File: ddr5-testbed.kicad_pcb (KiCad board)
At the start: 6 copper layers, 69.6 x 30 mm, 64 parts, among them IC1 PCA6408APW, IC2 AT24CS01, J1 ddr4-sodimm-edge-connector, U1 MT60B2G8HB-48B_A, U2 TPS613221ADBVT

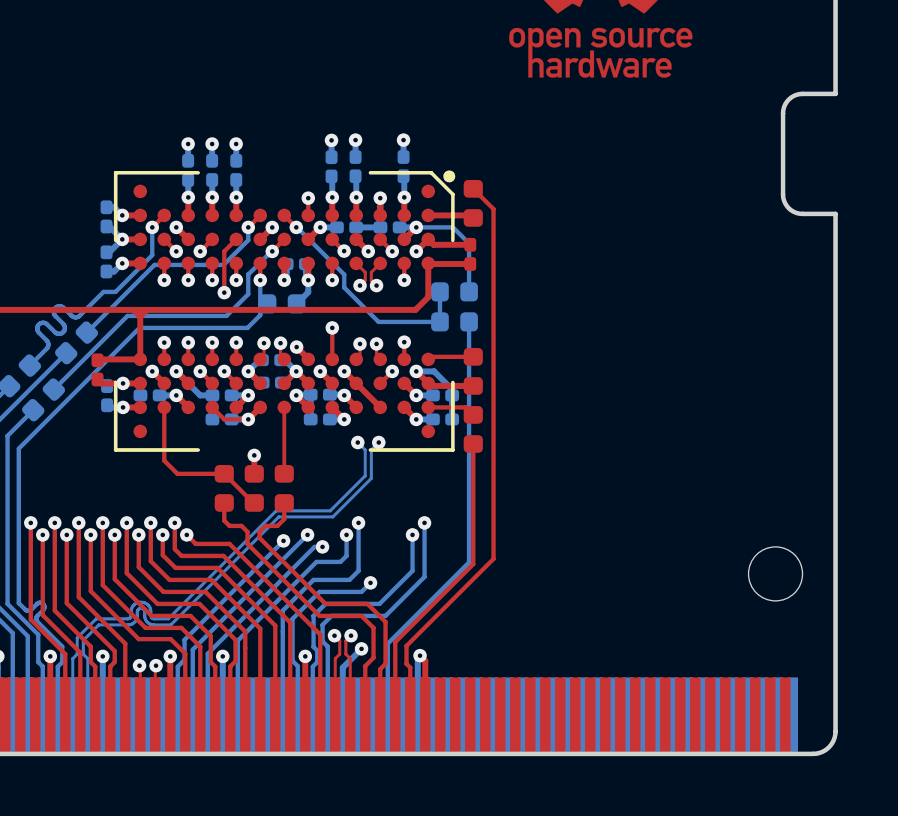
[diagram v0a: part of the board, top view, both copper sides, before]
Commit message: Tune LBDQ traces
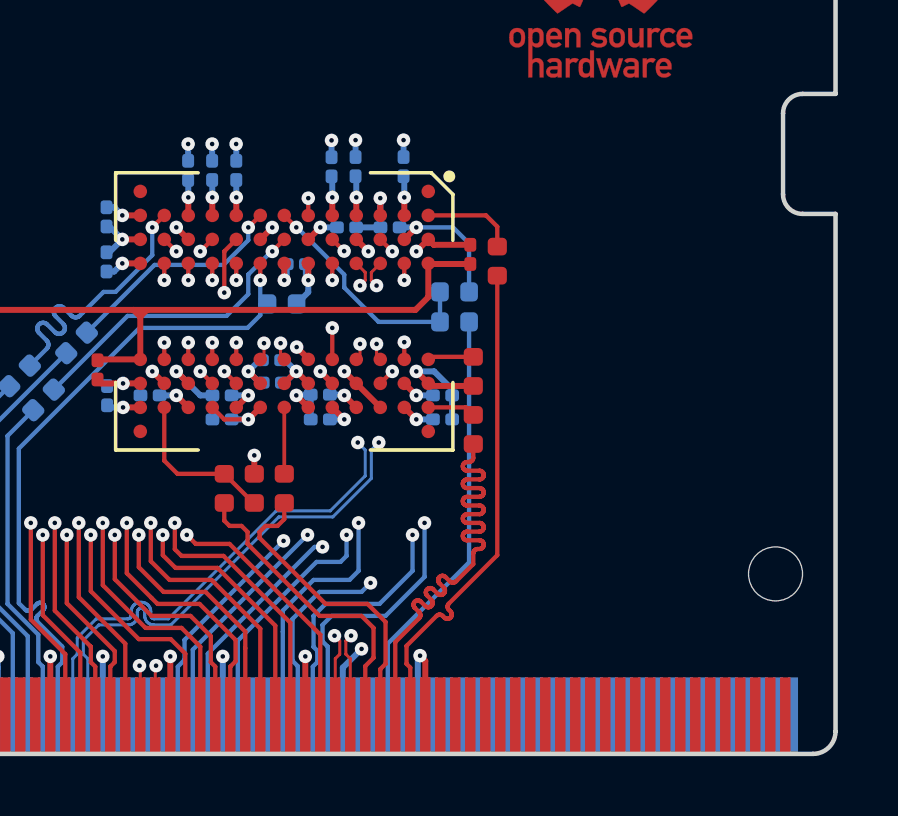
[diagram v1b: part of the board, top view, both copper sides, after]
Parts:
- moved R18 2.08 mm to (158.3, 83.6), turned to 270 degrees
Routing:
- net LBDQS: track 10.1 -> 18.0 mm
- net LBDQ: track 19.1 -> 16.4 mm
- net /DDR5/R_LBDQ: track 1.54 -> 3.12 mm

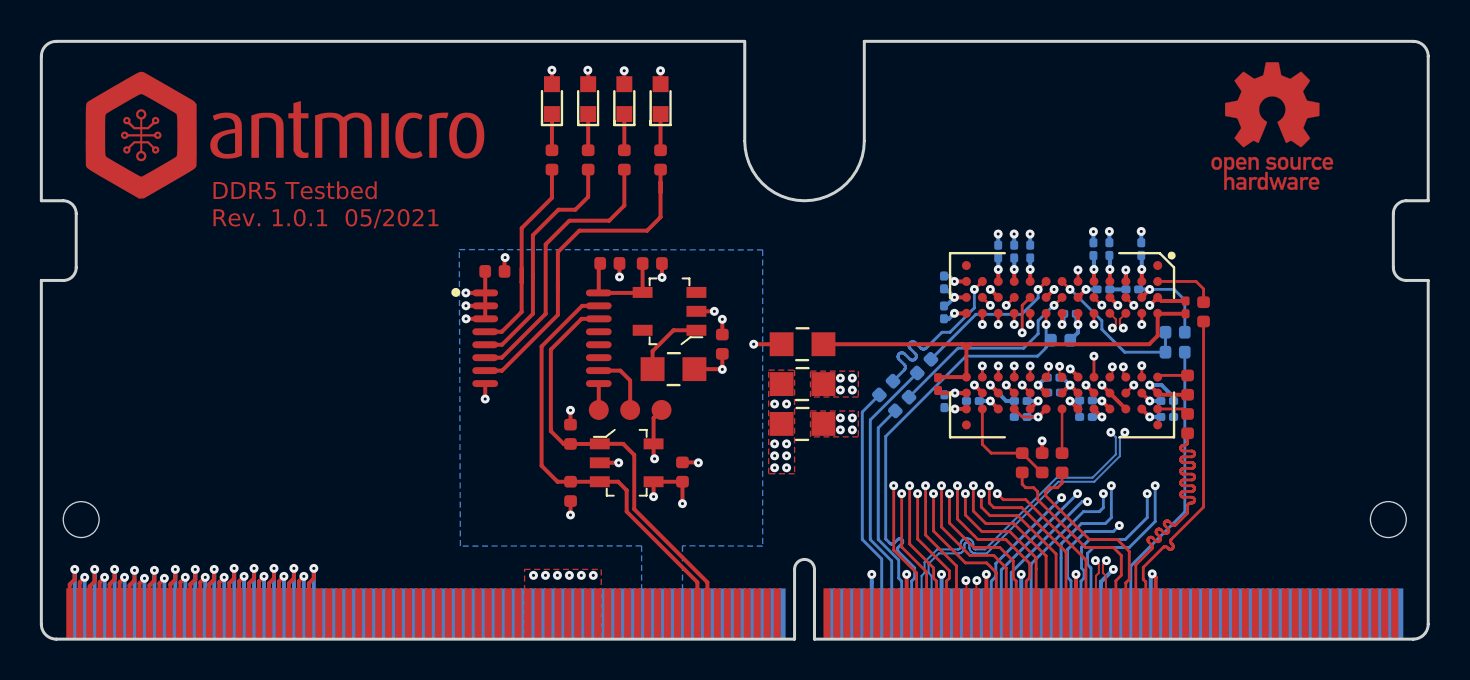
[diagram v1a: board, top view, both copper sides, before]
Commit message: Silks cleanup, fix date text
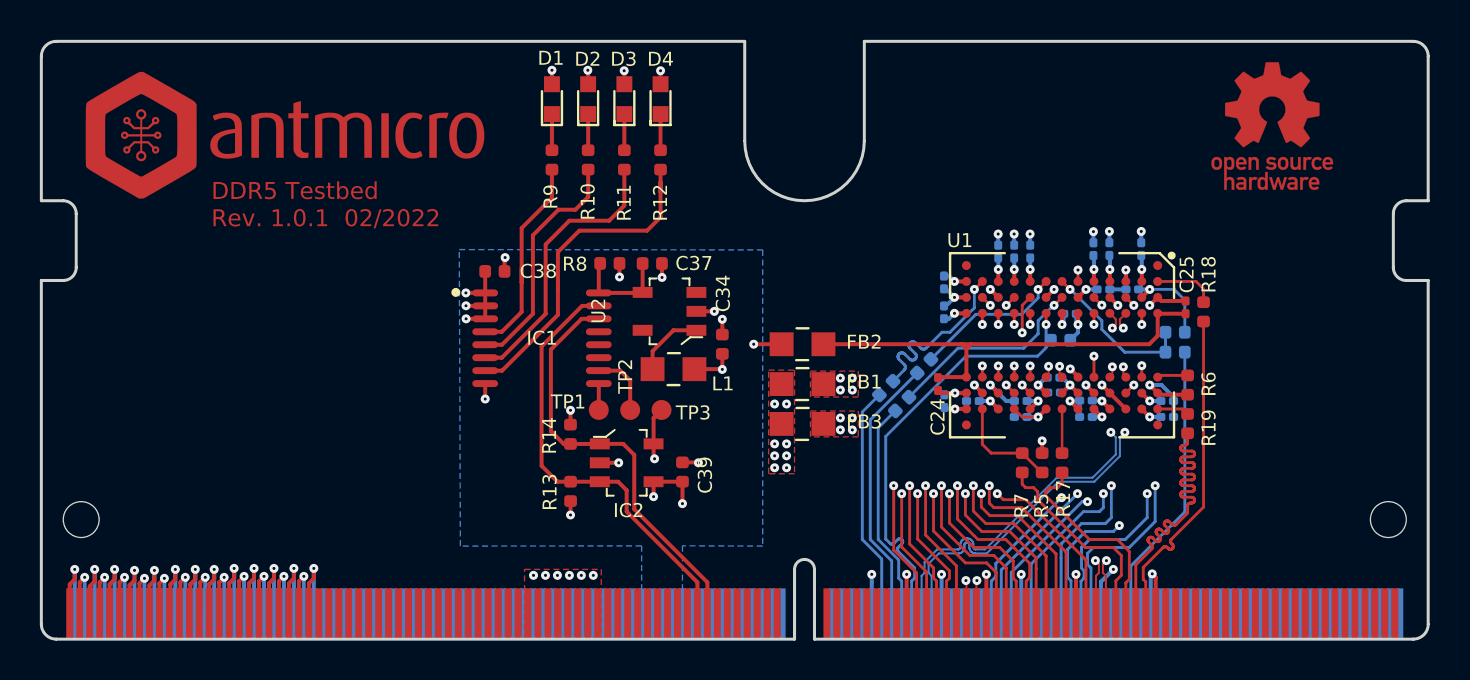
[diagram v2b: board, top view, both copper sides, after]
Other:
- board text added: "DDR5 Testbed Rev. 1.0.1 02/2022"
- board text removed: "DDR5 Testbed Rev. 1.0.1 05/2021"

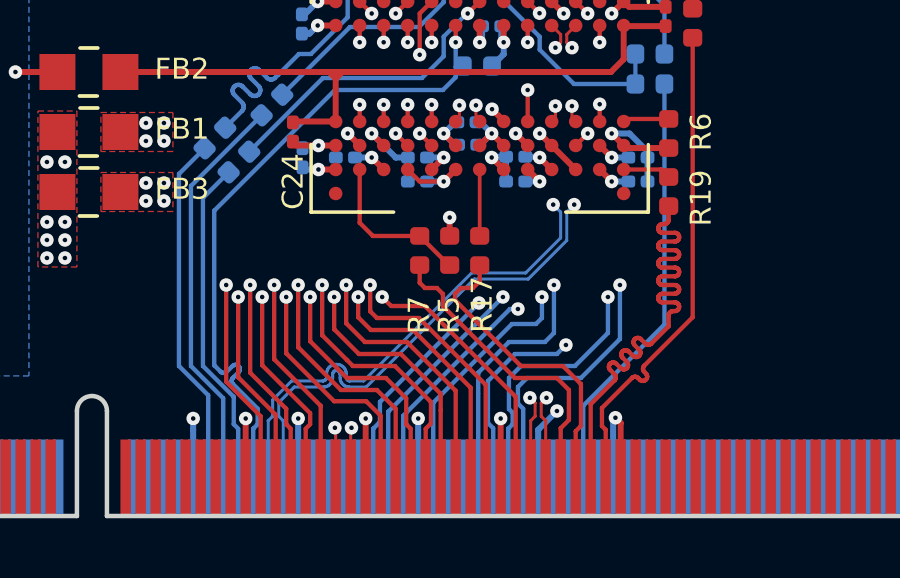
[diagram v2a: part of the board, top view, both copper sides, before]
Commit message: Change pullup resistors to 1K
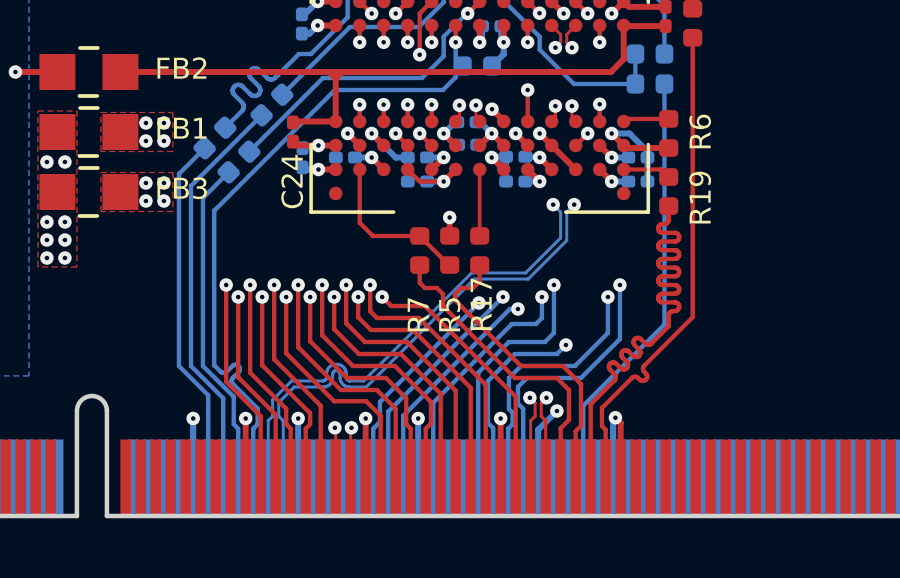
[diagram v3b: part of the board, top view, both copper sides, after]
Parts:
- R1, R5: value R_10k_0402 -> R_1k_0402

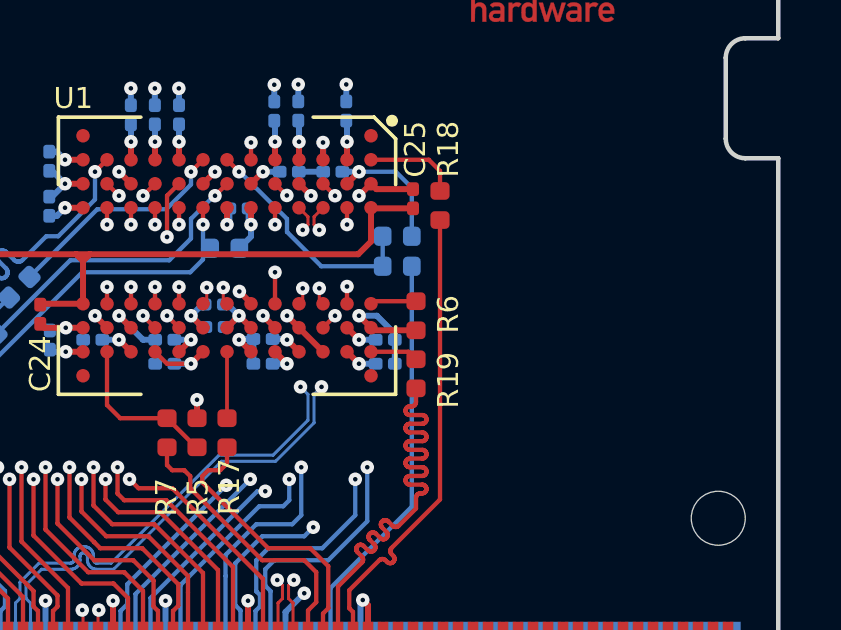
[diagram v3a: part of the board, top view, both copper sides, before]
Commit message: Change R6 to 1% tolerance
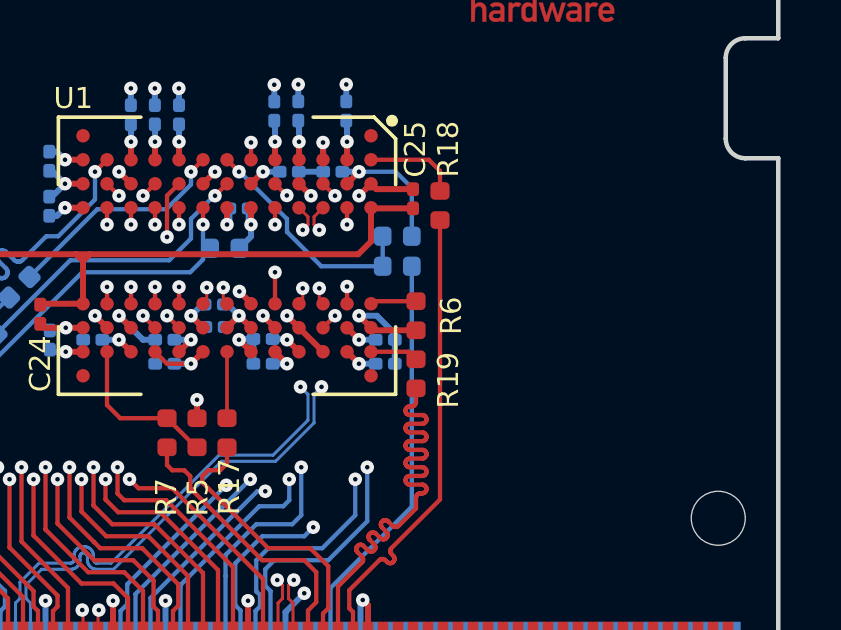
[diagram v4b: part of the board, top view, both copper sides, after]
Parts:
- R6: value R_240R_0402 -> R_240R_1%_0402
